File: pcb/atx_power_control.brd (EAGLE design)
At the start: 86 x 70 mm, 61 parts, among them IC2 REG1117, IC3 STM32F042F4, IC4 MY_7905DT, J1 ATX24RH, SW1 324_SW, SW2 324_SW, SW3 324_SW, SW4 324_SW, SW5 324_SW, SW7 324_SW, U1 USBC_16P, U2 USBC_16P

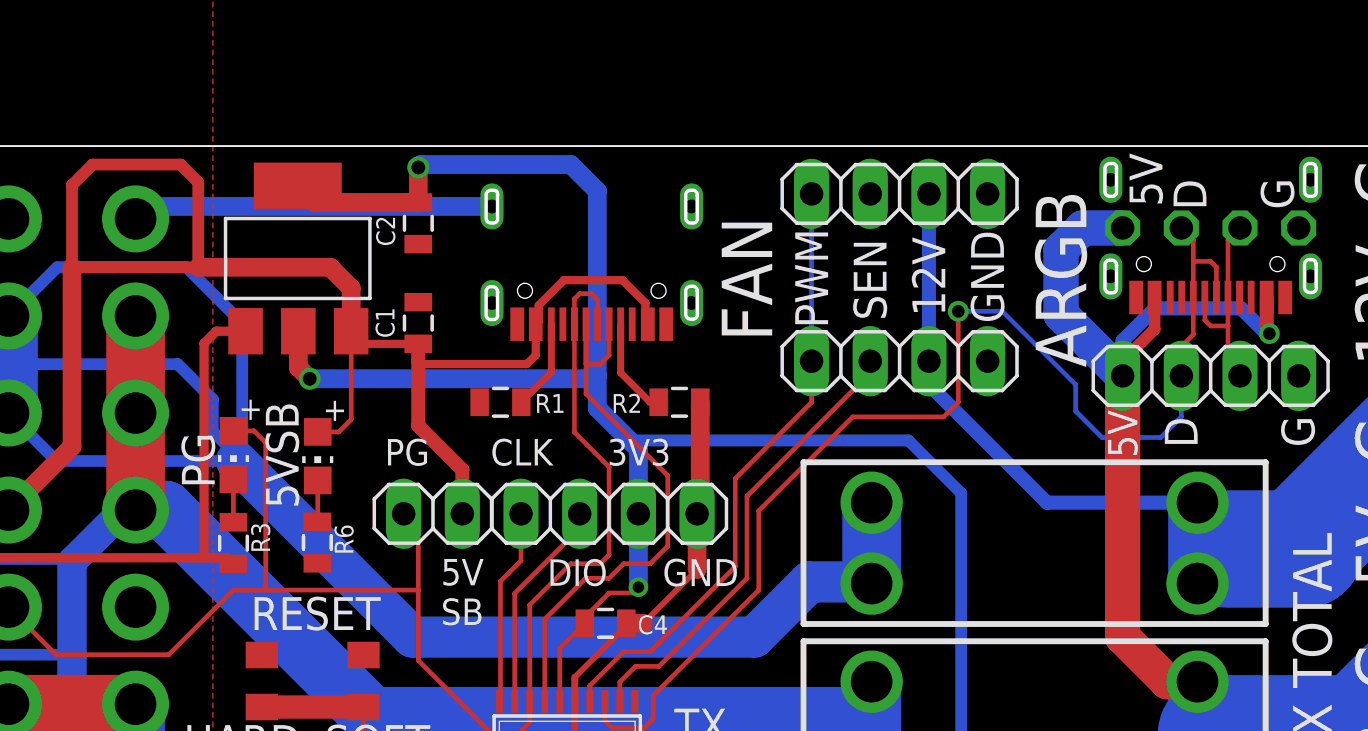
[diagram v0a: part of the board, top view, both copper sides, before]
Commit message: added ds18b20 header
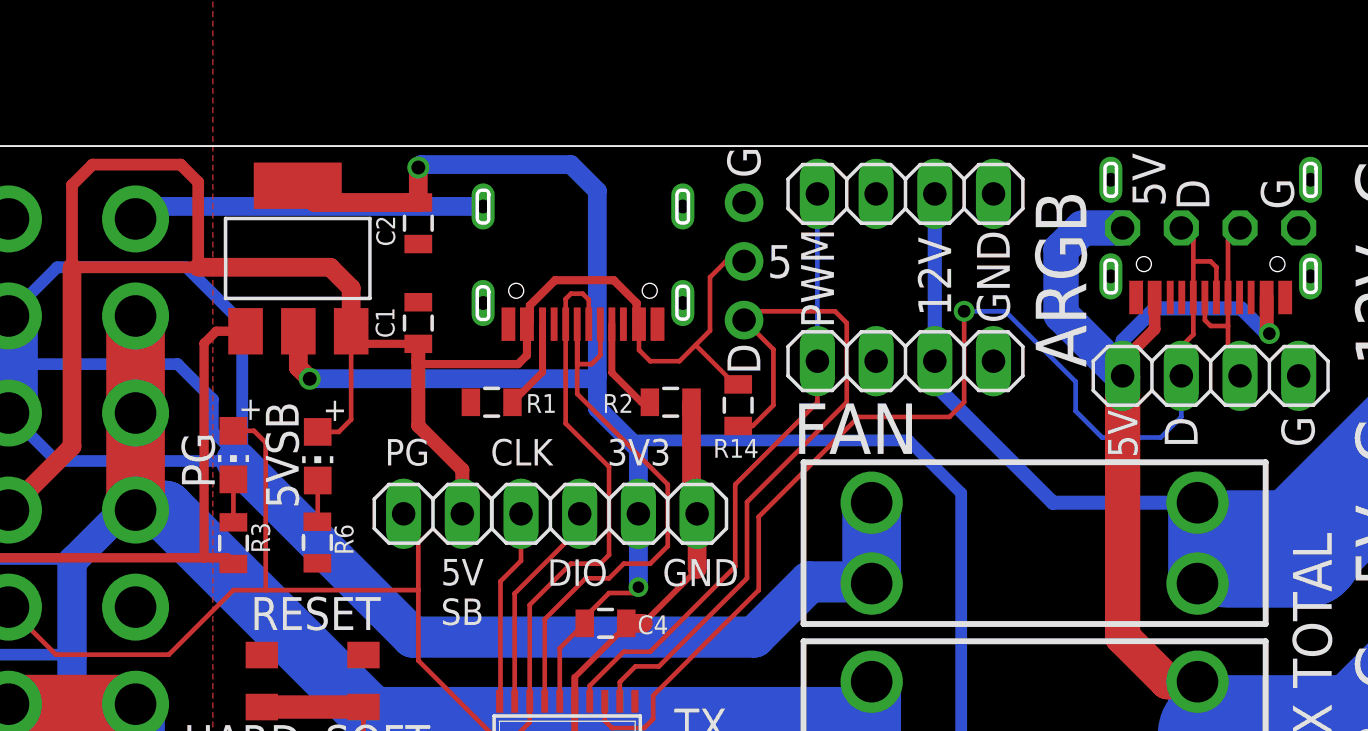
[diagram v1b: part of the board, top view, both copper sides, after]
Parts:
- added JP11: (no value), adafruit_changed:1X03-CLEANBIG
- added R14: 5k1, SparkFun-Passives:0805
- moved R1 0.38 mm to (34.9, 50.2)
- moved R2 0.38 mm to (42.7, 50.2)
- moved U2 0.38 mm to (38.9, 57.4)
- moved JP2 0.25 mm to (52.8, 51.9)
- moved JP4 0.25 mm to (52.8, 59.2)
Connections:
- net GND: now also JP11.3
- net N$6: now also JP11.1, R14.1; no longer JP2.2
- net VCC: now also JP11.2, R14.2
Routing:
- net N$6: track 19.8 -> 32.0 mm
- net VCC: track 70.2 -> 81.4 mm
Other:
- board text added: "5"
- board text removed: "SEN"

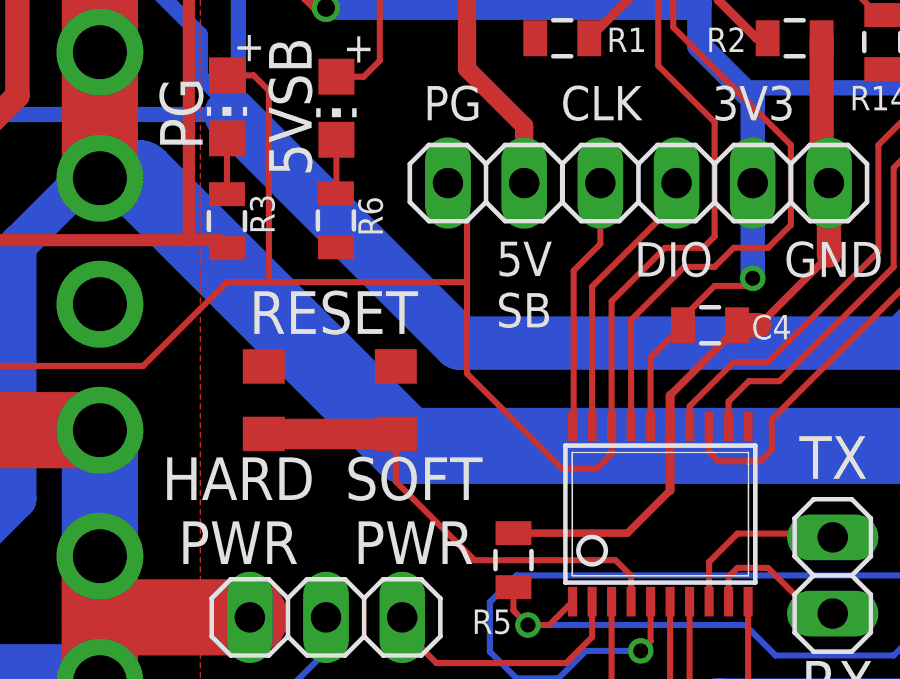
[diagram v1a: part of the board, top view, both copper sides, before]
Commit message: added indicator LED
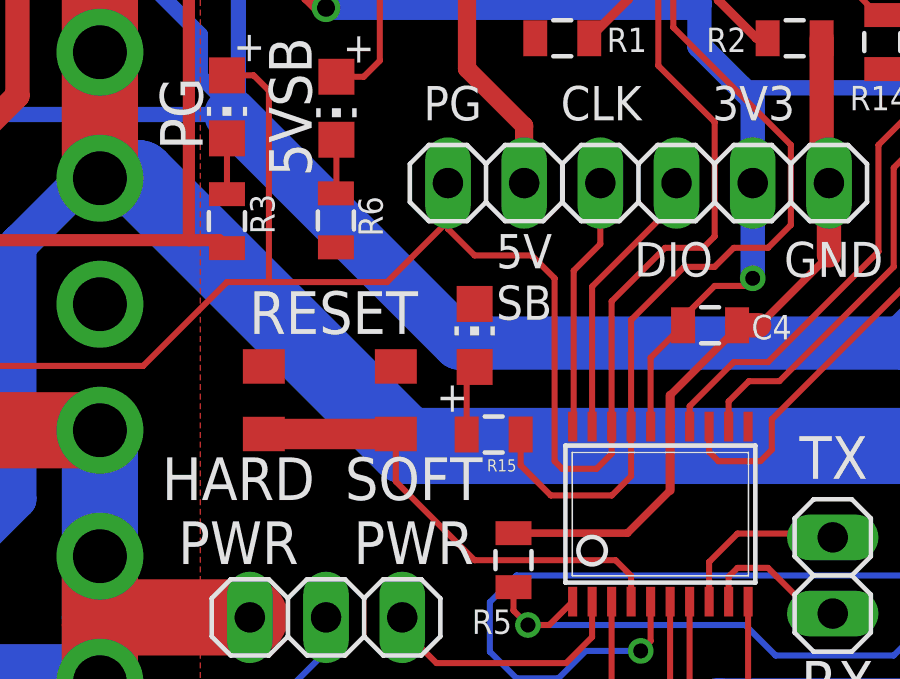
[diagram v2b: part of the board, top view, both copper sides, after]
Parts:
- added LED8: (no value), adafruit:CHIP-LED0805
- added R15: 5k1, SparkFun-Passives:0805
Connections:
- new net N$19: LED8.A, R15.2
- net GND: now also LED8.C
- net USB_DN: now also R15.1
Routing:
- net USB_DN: track 25.6 -> 32.7 mm
- net N$19: track 0.00 -> 2.36 mm
- net PG: track 64.2 -> 65.5 mm
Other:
- board text added: "ATX4VC.com dekuNukem SEPT 2022 PD1"
- board text removed: "ATX4VC.com dekuNukem SEPT 2022 PT5"
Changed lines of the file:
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@@
 <text x="73.406" y="27.686" size="2.1844" layer="25" rot="R270" align="center">G</text>
 <text x="76.835" y="18.796" size="2.1844" layer="25" rot="R270" align="center">G</text>
-<text x="33.655" y="41.9562" size="1.143" layer="25" rot="R180" align="center">5V
+<text x="33.655" y="42.2102" size="1.143" layer="25" rot="R180" align="center">5V
 SB</text>
 <text x="6.096" y="35.052" size="2.54" layer="26" rot="MR90" align="center">ATX4VC.com
 dekuNukem SEPT 2022
-PT5</text>
+PD1</text>
 <text x="43.9712" y="42.7944" size="1.1684" layer="25" align="center">GND</text>
 <text x="41.3042" y="48.0014" size="1.143" layer="25" align="center">3V3</text>
@@
 <attribute name="VALUE" x="49.022" y="52.451" size="1.27" layer="27" rot="R90"/>
 </element>
+<element name="R15" library="SparkFun-Passives" package="0805" value="5k1" x="32.639" y="36.957" smashed="yes" rot="R180">
+<attribute name="NAME" x="33.401" y="36.1315" size="0.4064" layer="25" rot="R180"/>
+</element>
+<element name="LED8" library="adafruit" package="CHIP-LED0805" value="" x="32.004" y="40.259" smashed="yes">
+<attribute name="VALUE" x="34.544" y="38.989" size="1.27" layer="27" rot="R90"/>
+</element>
 </elements>
 <signals>
@@
 <contactref element="JP12" pad="4"/>
 <contactref element="JP11" pad="3"/>
+<contactref element="LED8" pad="C"/>
 </signal>
 <signal name="+3V3">
@@
 <wire x1="38.989" y1="42.545" x2="37.221" y2="40.777" width="0.2032" layer="1"/>
 <wire x1="37.221" y1="40.777" x2="37.221" y2="37.2218" width="0.2032" layer="1"/>
+<contactref element="R15" pad="1"/>
+<wire x1="37.221" y1="37.2218" x2="37.221" y2="35.57" width="0.2032" layer="1"/>
+<wire x1="37.221" y1="35.57" x2="36.576" y2="34.925" width="0.2032" layer="1"/>
+<wire x1="36.576" y1="34.925" x2="34.544" y2="34.925" width="0.2032" layer="1"/>
+<wire x1="33.539" y1="35.93" x2="33.539" y2="36.957" width="0.2032" layer="1"/>
+<wire x1="34.544" y1="34.925" x2="33.539" y2="35.93" width="0.2032" layer="1"/>
 </signal>
 <signal name="BUTTON1">
@@
 <wire x1="40.005" y1="47.371" x2="40.005" y2="43.561" width="0.2032" layer="1"/>
 <wire x1="38.354" y1="43.18" x2="36.571" y2="41.397" width="0.2032" layer="1"/>
-<wire x1="34.925" y1="35.814" x2="36.068" y2="35.814" width="0.2032" layer="1"/>
+<wire x1="36.068" y1="35.814" x2="34.925" y2="35.814" width="0.2032" layer="1"/>
 <wire x1="36.068" y1="35.814" x2="36.571" y2="36.317" width="0.2032" layer="1"/>
 <wire x1="36.571" y1="36.317" x2="36.571" y2="37.2218" width="0.2032" layer="1"/>
@@
 <contactref element="JP3" pad="1"/>
 <wire x1="14.014" y1="41.3" x2="16.071" y2="39.243" width="0.2032" layer="1"/>
-<wire x1="31.115" y1="45.339" x2="31.75" y2="44.704" width="0.2032" layer="1"/>
-<wire x1="31.75" y1="44.704" x2="31.75" y2="42.037" width="0.2032" layer="1"/>
-<wire x1="31.75" y1="42.037" x2="31.75" y2="38.989" width="0.2032" layer="1"/>
-<wire x1="31.75" y1="38.989" x2="34.925" y2="35.814" width="0.2032" layer="1"/>
 <wire x1="25.146" y1="48.421" x2="24.638" y2="48.929" width="0.2032" layer="1"/>
 <wire x1="23.749" y1="48.929" x2="24.638" y2="48.929" width="0.2032" layer="1"/>
@@
 <wire x1="23.749" y1="42.037" x2="20.955" y2="39.243" width="0.2032" layer="1"/>
 <wire x1="25.146" y1="42.037" x2="23.749" y2="42.037" width="0.2032" layer="1"/>
-<wire x1="25.146" y1="42.037" x2="31.75" y2="42.037" width="0.2032" layer="1"/>
+<wire x1="31.115" y1="44.069" x2="29.083" y2="42.037" width="0.2032" layer="1"/>
+<wire x1="29.083" y1="42.037" x2="25.146" y2="42.037" width="0.2032" layer="1"/>
+<wire x1="34.925" y1="35.814" x2="34.671" y2="36.068" width="0.2032" layer="1"/>
+<wire x1="34.671" y1="42.164" x2="33.909" y2="42.926" width="0.2032" layer="1"/>
+<wire x1="33.909" y1="42.926" x2="32.004" y2="42.926" width="0.2032" layer="1"/>
+<wire x1="31.115" y1="43.815" x2="31.115" y2="45.339" width="0.2032" layer="1"/>
+<wire x1="34.671" y1="36.068" x2="34.671" y2="42.164" width="0.2032" layer="1"/>
+<wire x1="32.004" y1="42.926" x2="31.115" y2="43.815" width="0.2032" layer="1"/>
+<wire x1="31.115" y1="44.069" x2="31.115" y2="45.339" width="0" layer="19" extent="1-1"/>
 </signal>
 <signal name="N$30">
@@
 <wire x1="76.073" y1="28.194" x2="66.602" y2="28.194" width="5.08" layer="16"/>
 </signal>
+<signal name="N$19">
+<contactref element="R15" pad="2"/>
+<contactref element="LED8" pad="A"/>
+<wire x1="32.004" y1="39.209" x2="31.739" y2="38.944" width="0.2032" layer="1"/>
+<wire x1="31.739" y1="38.944" x2="31.739" y2="36.957" width="0.2032" layer="1"/>
+</signal>
 </signals>
